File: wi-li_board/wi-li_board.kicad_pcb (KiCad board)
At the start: 2 copper layers, 20.8 x 79.6 mm, 30 parts, among them J1 Barrel_Jack_MountingPin, J2 2059-302/998-403, J3 2059-302/998-403, J4 2059-302/998-403, Q1 Q_NMOS_DGS, Q2 Q_NMOS_DGS, Q3 Q_NMOS_DGS, U1 AP1509, U2 ESP-12E

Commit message: fix issues from first rev
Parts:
- added R10: 330, Resistor_SMD:R_0805_2012Metric_Pad1.20x1.40mm_HandSolder, F.Cu at (149.8, 105.5)
- added R11: 10k, Resistor_SMD:R_0805_2012Metric_Pad1.20x1.40mm_HandSolder, F.Cu at (145.8, 105.5)
- added R9: 10k, Resistor_SMD:R_0805_2012Metric_Pad1.20x1.40mm_HandSolder, F.Cu at (145.8, 97.6)
- L1: footprint Inductor_SMD:L_Vishay_IFSC-1515AH_4x4x1.8mm -> RLC:L_Vishay_IFSC-1515AH_HandSolder
- R1: value 10k -> 330
- R3, R7: value 330 -> 10k
- moved F2 39.5 mm to (150.5, 122.8), turned to 180 degrees
- moved C1 32.3 mm to (138.5, 112.4)
- moved C2 32.3 mm to (140.6, 112.4)
- moved C3 32.3 mm to (145.6, 118.2)
- moved C4 32.3 mm to (145.6, 120.4)
- moved U1 32.3 mm to (144.4, 112.4)
- moved L1 32.1 mm to (139.3, 118.7)
- moved R8 30.7 mm to (148.0, 79.7), turned to 90 degrees
- moved F1 27.8 mm to (135.6, 117.2), turned to -90 degrees
- moved R7 27.7 mm to (145.8, 79.7), turned to 90 degrees
- moved R6 23.7 mm to (150.2, 79.7), turned to 90 degrees
- moved D1 22.2 mm to (135.6, 111.8), turned to 90 degrees
- moved R3 16.0 mm to (141.4, 79.7), turned to 90 degrees
- moved R1 15.1 mm to (149.8, 89.5)
- moved J1 12.6 mm to (143.9, 128.4), turned to 0 degrees
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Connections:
- C1 pad 2: Net-(C1-Pad2) -> Net-(D1-Pad1)
- C2 pad 1: Net-(C1-Pad2) -> Net-(D1-Pad1)
- F1 pad 1: Net-(C1-Pad2) -> Net-(D1-Pad1)
- Q1 pad 1: Net-(F3-Pad1) -> Net-(Q1-Pad1)
- Q1 pad 2: Net-(Q1-Pad2) -> GND
- Q1 pad 3: GND -> Net-(F3-Pad1)
- Q2 pad 1: Net-(F4-Pad1) -> Net-(Q2-Pad1)
- Q2 pad 2: Net-(Q2-Pad2) -> GND
- Q2 pad 3: GND -> Net-(F4-Pad1)
- Q3 pad 1: Net-(F5-Pad1) -> Net-(Q3-Pad1)
- Q3 pad 2: Net-(Q3-Pad2) -> GND
- Q3 pad 3: GND -> Net-(F5-Pad1)
- R1 pad 1: VDD -> Net-(Q1-Pad1)
- R1 pad 2: Net-(R1-Pad2) -> GPIO_4
- R3 pad 1: Net-(Q1-Pad2) -> VDD
- R3 pad 2: GPIO_4 -> Net-(R3-Pad2)
- R4 pad 2: Net-(Q1-Pad2) -> Net-(Q1-Pad1)
- R5 pad 1: Net-(Q2-Pad2) -> Net-(Q2-Pad1)
- R6 pad 2: Net-(Q2-Pad2) -> Net-(R6-Pad2)
- R7 pad 1: Net-(Q3-Pad2) -> VDD
- R7 pad 2: GPIO_14 -> Net-(R7-Pad2)
- R8 pad 1: GND -> VDD
- R8 pad 2: Net-(Q3-Pad2) -> Net-(R8-Pad2)
- U1 pad 1: Net-(C1-Pad2) -> Net-(D1-Pad1)
- U2 pad 1: Net-(R1-Pad2) -> Net-(R2-Pad2)
- U2 pad 13: GPIO_4 -> unconnected-(U2-Pad13)
- U2 pad 14: GPIO_5 -> unconnected-(U2-Pad14)
- U2 pad 15: GPIO_3 -> GND
- U2 pad 16: unconnected-(U2-Pad16) -> Net-(R6-Pad2)
- U2 pad 17: unconnected-(U2-Pad17) -> Net-(R8-Pad2)
- U2 pad 18: unconnected-(U2-Pad18) -> Net-(R7-Pad2)
- U2 pad 19: GPIO9 -> GPIO_4
- U2 pad 20: GPIO10 -> unconnected-(U2-Pad20)
- U2 pad 3: Net-(R2-Pad2) -> Net-(R3-Pad2)
- U2 pad 4: GPIO_16 -> unconnected-(U2-Pad4)
- U2 pad 7: GPIO_13 -> unconnected-(U2-Pad7)
- U2 pad 9: GND -> unconnected-(U2-Pad9)
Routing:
- net VDD: track 13.0 -> 64.7 mm
- net Net-(R1-Pad2): track 28.5 -> 0.00 mm
- net Net-(C1-Pad2): track 20.1 -> 0.00 mm, vias 6 -> 0
- net Net-(R3-Pad2): track 0.00 -> 19.9 mm, vias 0 -> 2
- net Net-(R7-Pad2): track 0.00 -> 14.7 mm, vias 0 -> 2
- net GPIO_4: track 21.7 -> 34.7 mm
- net Net-(R8-Pad2): track 0.00 -> 12.9 mm, vias 0 -> 2
- net Net-(R6-Pad2): track 0.00 -> 11.2 mm, vias 0 -> 2
- net VCC: track 65.7 -> 76.5 mm
- net GND: track 21.1 -> 13.8 mm, vias 24 -> 33
- net GPIO_14: track 50.6 -> 57.8 mm
- net Net-(Q3-Pad2): track 6.06 -> 0.00 mm
- net Net-(Q1-Pad2): track 6.04 -> 0.00 mm
- net Net-(Q2-Pad2): track 5.95 -> 0.00 mm
- net Net-(D1-Pad1): track 12.9 -> 18.0 mm, vias 2 -> 0
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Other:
- board size 20.8 x 79.6 mm -> 25 x 88 mm

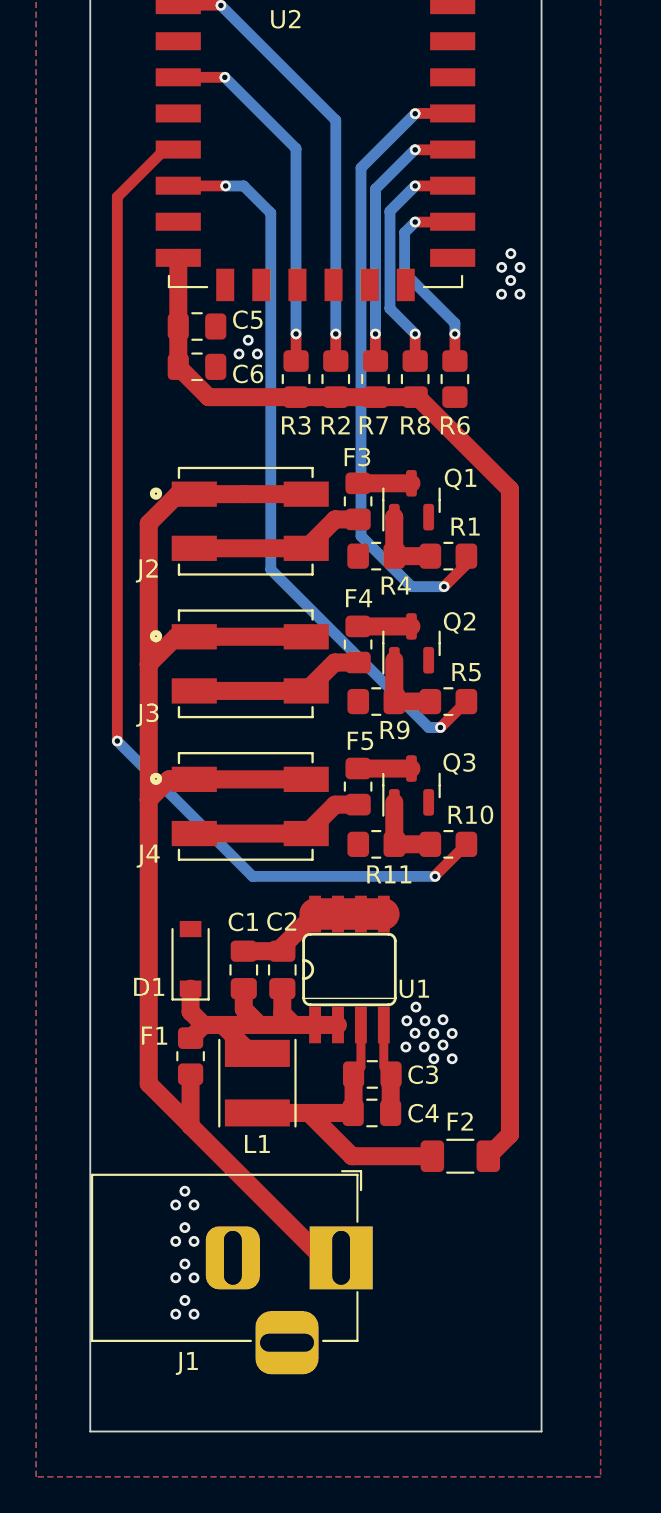
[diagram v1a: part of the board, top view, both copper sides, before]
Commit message: add current measurement and do most of the layout, plus fix voltage regulator mistake
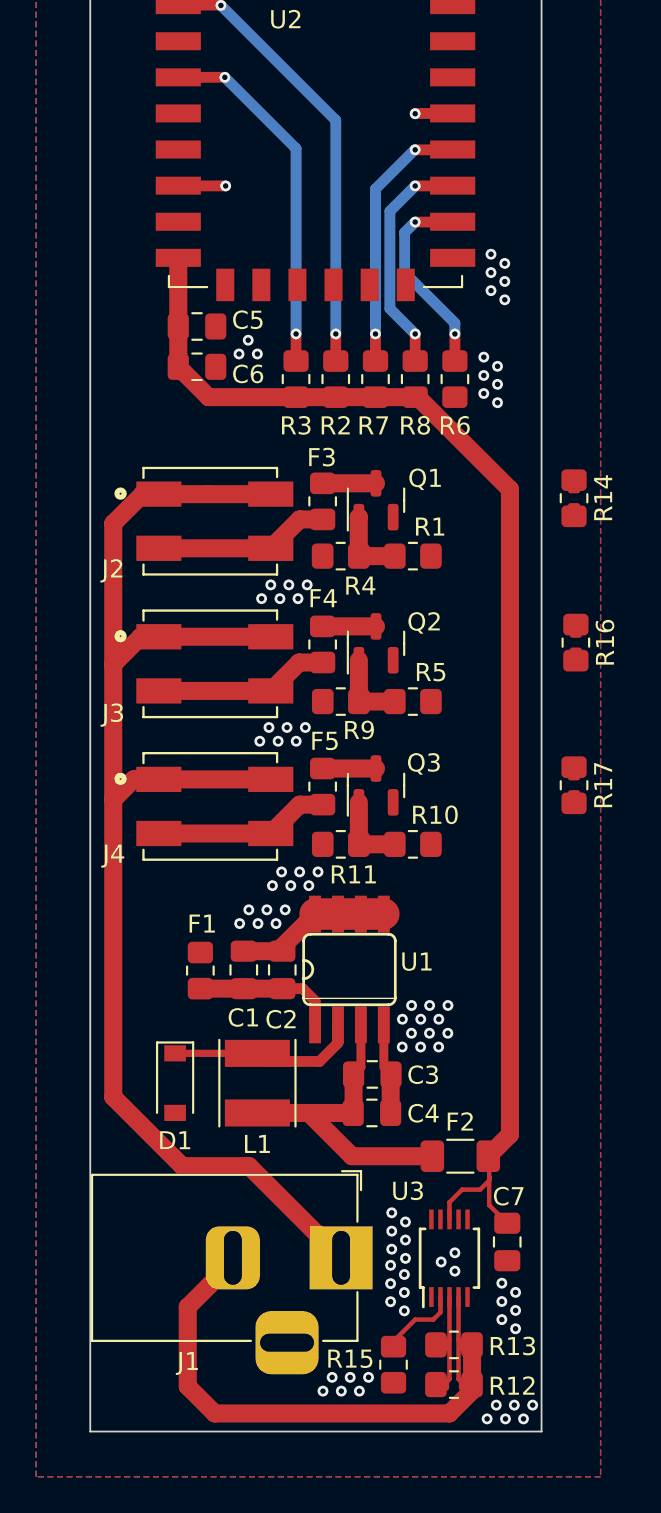
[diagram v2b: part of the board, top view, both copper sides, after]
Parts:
- added C7: 100n, Capacitor_SMD:C_0805_2012Metric_Pad1.18x1.45mm_HandSolder, F.Cu at (153.1, 127.5)
- added R12: 50m, RLC:R_shunt_0805_2012Metric_Pad1.20x1.40mm_HandSolder, F.Cu at (150.2, 135.4)
- added R13: 50m, RLC:R_shunt_0805_2012Metric_Pad1.20x1.40mm_HandSolder, F.Cu at (150.2, 133.2)
- added R14: 50m, RLC:R_shunt_0805_2012Metric_Pad1.20x1.40mm_HandSolder, F.Cu at (156.8, 86.3)
- added R15: 10k, Resistor_SMD:R_0805_2012Metric_Pad1.20x1.40mm_HandSolder, F.Cu at (146.8, 134.3)
- added R16: 50m, RLC:R_shunt_0805_2012Metric_Pad1.20x1.40mm_HandSolder, F.Cu at (156.9, 94.3)
- added R17: 50m, RLC:R_shunt_0805_2012Metric_Pad1.20x1.40mm_HandSolder, F.Cu at (156.8, 102.2)
- added U3: ADS1115IDGS, Package_SO:TSSOP-10_3x3mm_P0.5mm, F.Cu at (149.9, 128.4)
- moved D1 6.94 mm to (134.7, 118.7), turned to -90 degrees
- moved F1 4.77 mm to (136.1, 112.5), turned to 90 degrees
- moved F3 1.96 mm to (142.9, 86.5)
- moved F4 1.96 mm to (142.9, 94.4)
- moved F5 1.96 mm to (142.9, 102.3)
- moved J2 1.96 mm to (136.9, 87.6)
- moved J3 1.96 mm to (136.9, 95.5)
- moved J4 1.96 mm to (136.9, 103.4)
- moved R1 1.96 mm to (147.9, 89.5)
- moved R10 1.96 mm to (147.9, 105.5)
- moved R11 1.96 mm to (143.9, 105.5)
- moved R4 1.96 mm to (143.9, 89.5)
- moved R5 1.96 mm to (147.9, 97.6)
- moved R9 1.96 mm to (143.9, 97.6)
- moved Q1 1.96 mm to (145.8, 86.4)
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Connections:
- net GPIO_12 renamed OUT_CTRL_2
- net GPIO_14 renamed OUT_CTRL_3
- net GPIO_4 renamed OUT_CTRL_1
- C1 pad 2: Net-(D1-Pad1) -> Net-(C1-Pad2)
- C2 pad 1: Net-(D1-Pad1) -> Net-(C1-Pad2)
- F1 pad 1: Net-(D1-Pad1) -> Net-(C1-Pad2)
- J1 pad 2: GND -> Net-(J1-Pad2)
- Q1 pad 2: GND -> Net-(Q1-Pad2)
- Q2 pad 2: GND -> Net-(Q2-Pad2)
- Q3 pad 2: GND -> Net-(Q3-Pad2)
- U1 pad 1: Net-(D1-Pad1) -> Net-(C1-Pad2)
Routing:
- net OUT_CTRL_3: track 57.8 -> 0.00 mm, vias 2 -> 0
- net OUT_CTRL_2: track 40.6 -> 2.63 mm, vias 2 -> 1
- net OUT_CTRL_1: track 34.7 -> 2.08 mm, vias 2 -> 1
- net Net-(J1-Pad2): track 0.00 -> 27.6 mm
- net VDD: track 64.7 -> 72.7 mm
- net Net-(C1-Pad2): track 0.00 -> 7.96 mm
- net Net-(D1-Pad1): track 18.0 -> 10.6 mm
- net I_SENSE_VCC_NEG: track 0.00 -> 5.45 mm, vias 0 -> 6
- net I_SENSE_VCC_POS: track 0.00 -> 5.40 mm
- net Net-(R15-Pad2): track 0.00 -> 4.41 mm
- net VCC: track 76.5 -> 77.1 mm
- net GND: vias 33 -> 78
- added copper zone on B.Cu, net I_SENSE_VCC_NEG
- added copper zone on F.Cu, net I_SENSE_VCC_NEG
- removed copper zone on B.Cu, net GND
- removed copper zone on F.Cu, net GND

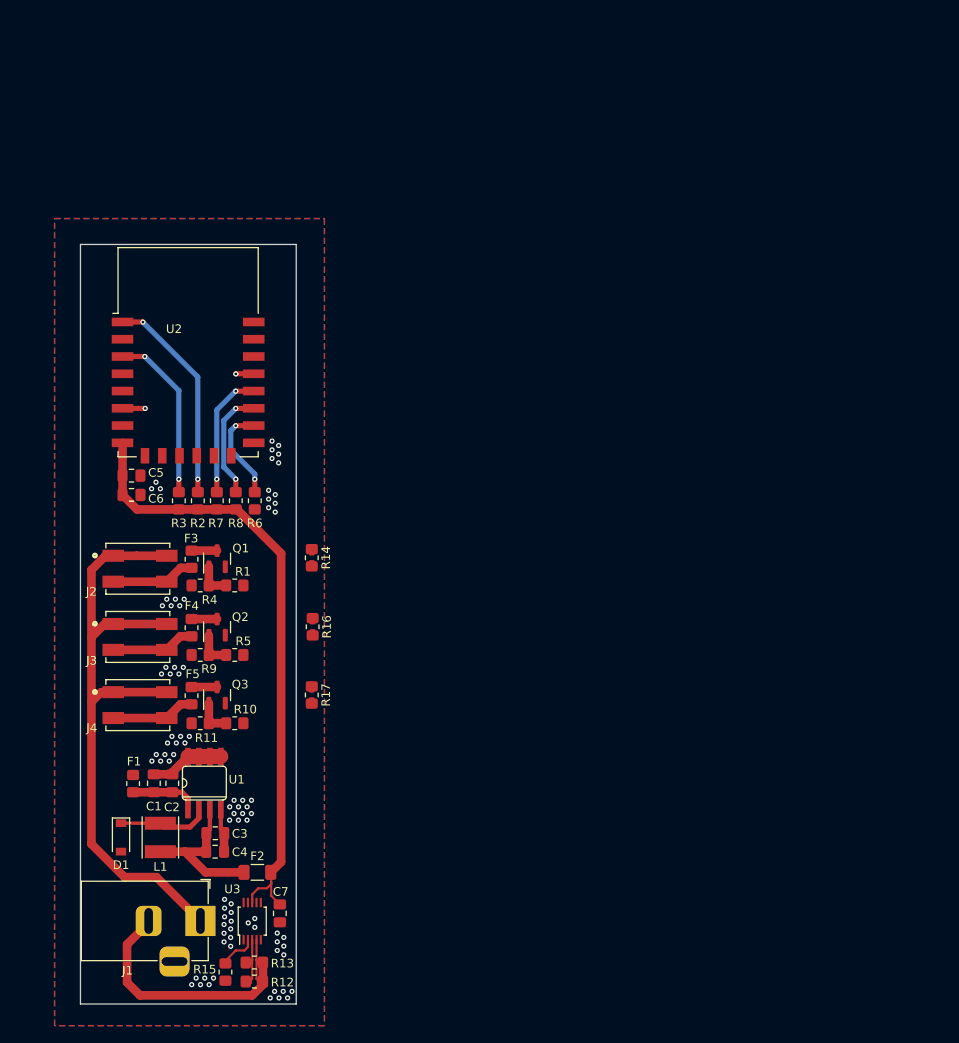
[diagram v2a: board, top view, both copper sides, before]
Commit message: Circular Board   - Fix mistake on voltage regulator from previous version   - Add ADC IC   - Add current measurement to all three channels and input using ADC IC   - Add programming header   - Switch to XT-30 connectors instead of Wago   - Panelize
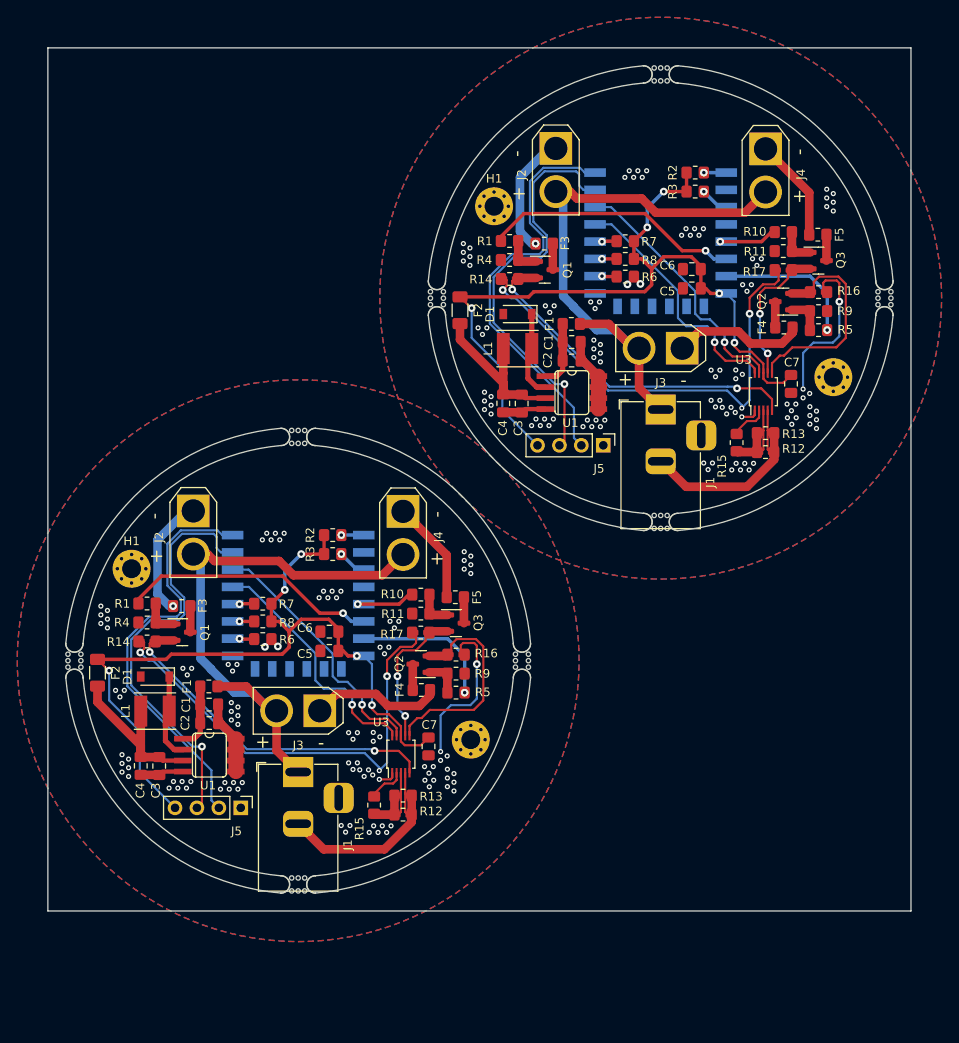
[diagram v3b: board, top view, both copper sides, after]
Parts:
- removed the C1 at (138.5, 112.4)
- removed the C2 at (140.6, 112.4)
- removed the C3 at (145.6, 118.2)
- removed the C4 at (145.6, 120.4)
- removed the C5 at (135.9, 76.8)
- removed the C6 at (135.9, 79.0)
- removed the C7 at (153.1, 127.5)
- removed the D1 at (134.7, 118.7)
- removed the F1 at (136.1, 112.5)
- removed the F2 at (150.5, 122.8)
- removed the L1 at (139.3, 118.7)
- removed the R12 at (150.2, 135.4)
- removed the R13 at (150.2, 133.2)
- removed the R15 at (146.8, 134.3)
- removed the R2 at (143.6, 79.7)
- removed the R3 at (141.4, 79.7)
- removed the R6 at (150.2, 79.7)
- removed the R7 at (145.8, 79.7)
- removed the R8 at (148.0, 79.7)
- removed the U1 at (144.4, 112.4)
- removed the U3 at (149.9, 128.4)
- added C1: 10n, Capacitor_SMD:C_0805_2012Metric_Pad1.18x1.45mm_HandSolder, F.Cu at (186.9, 61.3)
- added C1: 10n, Capacitor_SMD:C_0805_2012Metric_Pad1.18x1.45mm_HandSolder, F.Cu at (144.9, 103.3)
- added C2: 100n, Capacitor_SMD:C_0805_2012Metric_Pad1.18x1.45mm_HandSolder, F.Cu at (144.9, 105.4)
- added C2: 100n, Capacitor_SMD:C_0805_2012Metric_Pad1.18x1.45mm_HandSolder, F.Cu at (186.9, 63.4)
- added C3: 10n, Capacitor_SMD:C_0805_2012Metric_Pad1.18x1.45mm_HandSolder, F.Cu at (139.1, 110.4)
- added C3: 10n, Capacitor_SMD:C_0805_2012Metric_Pad1.18x1.45mm_HandSolder, F.Cu at (181.1, 68.4)
- added C4: 100n, Capacitor_SMD:C_0805_2012Metric_Pad1.18x1.45mm_HandSolder, F.Cu at (137.0, 110.4)
- added C4: 100n, Capacitor_SMD:C_0805_2012Metric_Pad1.18x1.45mm_HandSolder, F.Cu at (179.0, 68.4)
- added C5: 10n, Capacitor_SMD:C_0805_2012Metric_Pad1.18x1.45mm_HandSolder, F.Cu at (200.8, 55.1)
- added C5: 10n, Capacitor_SMD:C_0805_2012Metric_Pad1.18x1.45mm_HandSolder, F.Cu at (158.8, 97.1)
- added C6: 100n, Capacitor_SMD:C_0805_2012Metric_Pad1.18x1.45mm_HandSolder, F.Cu at (200.8, 52.9)
- added C6: 100n, Capacitor_SMD:C_0805_2012Metric_Pad1.18x1.45mm_HandSolder, F.Cu at (158.8, 94.9)
- added C7: 100n, Capacitor_SMD:C_0805_2012Metric_Pad1.18x1.45mm_HandSolder, F.Cu at (212.3, 66.2)
- added C7: 100n, Capacitor_SMD:C_0805_2012Metric_Pad1.18x1.45mm_HandSolder, F.Cu at (170.3, 108.2)
- added D1: MBRX120LF-TP, Diode_SMD:D_SOD-123, F.Cu at (138.6, 100.1)
- added D1: MBRX120LF-TP, Diode_SMD:D_SOD-123, F.Cu at (180.6, 58.1)
- added F1: 375m, Resistor_SMD:R_0805_2012Metric_Pad1.20x1.40mm_HandSolder, F.Cu at (186.9, 59.2)
- added F1: 375m, Resistor_SMD:R_0805_2012Metric_Pad1.20x1.40mm_HandSolder, F.Cu at (144.9, 101.2)
- added F2: 160m, Resistor_SMD:R_1206_3216Metric_Pad1.30x1.75mm_HandSolder, F.Cu at (174.0, 57.6)
- added F2: 160m, Resistor_SMD:R_1206_3216Metric_Pad1.30x1.75mm_HandSolder, F.Cu at (132.0, 99.6)
- added F3: 375m, Resistor_SMD:R_0805_2012Metric_Pad1.20x1.40mm_HandSolder, F.Cu at (183.7, 49.9)
- added F4: 375m, Resistor_SMD:R_0805_2012Metric_Pad1.20x1.40mm_HandSolder, F.Cu at (211.5, 59.6)
- added F5: 375m, Resistor_SMD:R_0805_2012Metric_Pad1.20x1.40mm_HandSolder, F.Cu at (215.4, 48.9)
- added H1: MountingHole_Pad, MountingHole:MountingHole_2.2mm_M2_Pad_Via, F.Cu at (135.9, 87.6)
- added H1: MountingHole_Pad, MountingHole:MountingHole_2.2mm_M2_Pad_Via, F.Cu at (177.9, 45.6)
- added H2: MountingHole_Pad, MountingHole:MountingHole_2.2mm_M2_Pad_Via, F.Cu at (217.2, 65.4)
- added H2: MountingHole_Pad, MountingHole:MountingHole_2.2mm_M2_Pad_Via, F.Cu at (175.2, 107.4)
- added J1: Barrel_Jack_MountingPin, Connector_BarrelJack:BarrelJack_Horizontal, F.Cu at (197.2, 69.1)
- added J2: XT30, Connector_AMASS:AMASS_XT30U-M_1x02_P5.0mm_Vertical, F.Cu at (185.1, 38.9)
- added J3: XT30, Connector_AMASS:AMASS_XT30U-M_1x02_P5.0mm_Vertical, F.Cu at (199.7, 62.0)
- added J4: XT30, Connector_AMASS:AMASS_XT30U-M_1x02_P5.0mm_Vertical, F.Cu at (209.4, 38.9)
- added J5: DBG, Connector_PinHeader_2.54mm:PinHeader_1x04_P2.54mm_Vertical, F.Cu at (190.6, 73.3)
- added J5: DBG, Connector_PinHeader_2.54mm:PinHeader_1x04_P2.54mm_Vertical, F.Cu at (148.6, 115.3)
- added L1: 47u, RLC:L_Vishay_IFSC-1515AH_HandSolder, F.Cu at (180.6, 62.1)
- added L1: 47u, RLC:L_Vishay_IFSC-1515AH_HandSolder, F.Cu at (138.6, 104.1)
- added Q1: Q_NMOS_DGS, Package_TO_SOT_SMD:SOT-23, F.Cu at (183.8, 52.9)
- added Q2: Q_NMOS_DGS, Package_TO_SOT_SMD:SOT-23, F.Cu at (211.4, 56.6)
- added Q3: Q_NMOS_DGS, Package_TO_SOT_SMD:SOT-23, F.Cu at (215.5, 51.9)
- added R1: 330, Resistor_SMD:R_0805_2012Metric_Pad1.20x1.40mm_HandSolder, F.Cu at (179.7, 49.6)
- added R10: 330, Resistor_SMD:R_0805_2012Metric_Pad1.20x1.40mm_HandSolder, F.Cu at (211.4, 48.6)
- added R11: 10k, Resistor_SMD:R_0805_2012Metric_Pad1.20x1.40mm_HandSolder, F.Cu at (211.4, 50.8)
- added R12: 50m, RLC:R_shunt_0805_2012Metric_Pad1.20x1.40mm_HandSolder, F.Cu at (167.4, 116.1)
- added R12: 50m, RLC:R_shunt_0805_2012Metric_Pad1.20x1.40mm_HandSolder, F.Cu at (209.4, 74.1)
- added R13: 50m, RLC:R_shunt_0805_2012Metric_Pad1.20x1.40mm_HandSolder, F.Cu at (167.4, 113.9)
- added R13: 50m, RLC:R_shunt_0805_2012Metric_Pad1.20x1.40mm_HandSolder, F.Cu at (209.4, 71.9)
- added R14: 50m, RLC:R_shunt_0805_2012Metric_Pad1.20x1.40mm_HandSolder, F.Cu at (179.7, 54.0)
- added R15: 10k, Resistor_SMD:R_0805_2012Metric_Pad1.20x1.40mm_HandSolder, F.Cu at (164.0, 115.0)
- added R15: 10k, Resistor_SMD:R_0805_2012Metric_Pad1.20x1.40mm_HandSolder, F.Cu at (206.0, 73.0)
- added R16: 50m, RLC:R_shunt_0805_2012Metric_Pad1.20x1.40mm_HandSolder, F.Cu at (215.5, 55.5)
- added R17: 50m, RLC:R_shunt_0805_2012Metric_Pad1.20x1.40mm_HandSolder, F.Cu at (211.4, 53.0)
- added R2: 10k, Resistor_SMD:R_0805_2012Metric_Pad1.20x1.40mm_HandSolder, F.Cu at (159.2, 83.7)
- added R2: 10k, Resistor_SMD:R_0805_2012Metric_Pad1.20x1.40mm_HandSolder, F.Cu at (201.2, 41.7)
- added R3: 10k, Resistor_SMD:R_0805_2012Metric_Pad1.20x1.40mm_HandSolder, F.Cu at (201.2, 43.9)
- added R3: 10k, Resistor_SMD:R_0805_2012Metric_Pad1.20x1.40mm_HandSolder, F.Cu at (159.2, 85.9)
- added R4: 10k, Resistor_SMD:R_0805_2012Metric_Pad1.20x1.40mm_HandSolder, F.Cu at (179.7, 51.8)
- added R5: 330, Resistor_SMD:R_0805_2012Metric_Pad1.20x1.40mm_HandSolder, F.Cu at (215.5, 59.9)
- added R6: 10k, Resistor_SMD:R_0805_2012Metric_Pad1.20x1.40mm_HandSolder, F.Cu at (151.1, 95.7)
- added R6: 10k, Resistor_SMD:R_0805_2012Metric_Pad1.20x1.40mm_HandSolder, F.Cu at (193.1, 53.7)
- added R7: 10k, Resistor_SMD:R_0805_2012Metric_Pad1.20x1.40mm_HandSolder, F.Cu at (151.1, 91.6)
- added R7: 10k, Resistor_SMD:R_0805_2012Metric_Pad1.20x1.40mm_HandSolder, F.Cu at (193.1, 49.6)
- added R8: 10k, Resistor_SMD:R_0805_2012Metric_Pad1.20x1.40mm_HandSolder, F.Cu at (193.1, 51.7)
- added R8: 10k, Resistor_SMD:R_0805_2012Metric_Pad1.20x1.40mm_HandSolder, F.Cu at (151.1, 93.7)
- added R9: 10k, Resistor_SMD:R_0805_2012Metric_Pad1.20x1.40mm_HandSolder, F.Cu at (215.5, 57.7)
- added U1: AP1509, Diodes_Inc:SO08, F.Cu at (144.9, 109.2)
- added U1: AP1509, Diodes_Inc:SO08, F.Cu at (186.9, 67.2)
- added U2: ESP-12E, RF_Module:ESP-12E, B.Cu at (197.2, 45.2)
- added U3: ADS1115IDGS, Package_SO:TSSOP-10_3x3mm_P0.5mm, F.Cu at (167.1, 109.1)
- added U3: ADS1115IDGS, Package_SO:TSSOP-10_3x3mm_P0.5mm, F.Cu at (209.1, 67.1)
- added mouse-bite-2mm-slot: VAL**, Panelization:mouse-bite-2mm-slot, F.Cu at (197.2, 82.2)
- added mouse-bite-2mm-slot: VAL**, Panelization:mouse-bite-2mm-slot, F.Cu at (171.3, 56.2)
- added mouse-bite-2mm-slot: VAL**, Panelization:mouse-bite-2mm-slot, F.Cu at (155.2, 124.2)
- added mouse-bite-2mm-slot: VAL**, Panelization:mouse-bite-2mm-slot, F.Cu at (181.2, 98.2)
- added mouse-bite-2mm-slot: VAL**, Panelization:mouse-bite-2mm-slot, F.Cu at (223.2, 56.2)
- added mouse-bite-2mm-slot: VAL**, Panelization:mouse-bite-2mm-slot, F.Cu at (197.2, 30.3)
- added mouse-bite-2mm-slot: VAL**, Panelization:mouse-bite-2mm-slot, F.Cu at (155.2, 72.3)
- added mouse-bite-2mm-slot: VAL**, Panelization:mouse-bite-2mm-slot, F.Cu at (129.3, 98.2)
- J2, J3, J4: value 2059-302/998-403 -> XT30; footprint Wago:WAGO_2059-302_998-403 -> Connector_AMASS:AMASS_XT30U-M_1x02_P5.0mm_Vertical
- U2: moved to B.Cu
- moved J4 37.9 mm to (167.4, 80.9), turned to -90 degrees
- moved F5 32.6 mm to (173.4, 90.9), turned to 180 degrees
- moved R9 29.7 mm to (173.5, 99.7), turned to 180 degrees
- moved Q3 28.9 mm to (173.5, 93.9), turned to 0 degrees
- moved R11 28.5 mm to (169.4, 92.8)
- moved U2 27.8 mm to (155.2, 87.2), turned to 180 degrees
- moved F4 27.6 mm to (169.5, 101.6), turned to 0 degrees
- moved R10 26.2 mm to (169.4, 90.6), turned to 180 degrees
- moved R5 26.0 mm to (173.5, 101.9)
- moved Q2 24.0 mm to (169.4, 98.6), turned to 180 degrees
- moved J3 22.5 mm to (157.7, 104.0), turned to 180 degrees
- moved R14 21.4 mm to (137.7, 96.0), turned to 0 degrees
- moved J1 20.6 mm to (155.2, 111.1), turned to 90 degrees
- moved R16 16.9 mm to (173.5, 97.5), turned to 180 degrees
- moved R17 14.6 mm to (169.4, 95.0), turned to 0 degrees
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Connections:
- J2 pad 1: VCC -> Net-(F3-Pad2)
- J2 pad 2: Net-(F3-Pad2) -> VCC
- J3 pad 1: VCC -> Net-(F4-Pad2)
- J3 pad 2: Net-(F4-Pad2) -> VCC
- J4 pad 1: VCC -> Net-(F5-Pad2)
- J4 pad 2: Net-(F5-Pad2) -> VCC
- U2 pad 19: OUT_CTRL_1 -> SCL
- U2 pad 20: unconnected-(U2-Pad20) -> SDA
- U2 pad 21: unconnected-(U2-Pad21) -> RX
- U2 pad 22: unconnected-(U2-Pad22) -> TX
- U2 pad 6: OUT_CTRL_2 -> OUT_CTRL_1
- U2 pad 7: unconnected-(U2-Pad7) -> OUT_CTRL_2
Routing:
- net GND: track 13.8 -> 196.4 mm, vias 78 -> 214
- net VDD: track 72.7 -> 180.2 mm, vias 0 -> 10
- net RX: track 0.00 -> 98.3 mm, vias 0 -> 2
- net TX: track 0.00 -> 97.0 mm
- net Net-(Q1-Pad2): track 0.00 -> 80.5 mm, vias 0 -> 4
- net SDA: track 0.00 -> 60.0 mm, vias 0 -> 2
- net SCL: track 0.00 -> 57.8 mm, vias 0 -> 2
- net OUT_CTRL_1: track 2.08 -> 59.8 mm, vias 1 -> 2
- net VCC: track 77.1 -> 132.5 mm
- net I_SENSE_MOS_2: track 0.00 -> 49.7 mm
- net Net-(Q3-Pad2): track 0.00 -> 33.5 mm, vias 0 -> 4
- net OUT_CTRL_2: track 2.63 -> 33.6 mm, vias 1 -> 2
- net Net-(C3-Pad2): track 18.2 -> 41.2 mm
- net Net-(F4-Pad2): track 9.73 -> 30.6 mm
- net Net-(J1-Pad2): track 27.6 -> 48.3 mm
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- added copper zone on B.Cu, net GND
- added copper zone on F.Cu, net GND
- removed copper zone on B.Cu, net I_SENSE_VCC_NEG
- removed copper zone on F.Cu, net I_SENSE_VCC_NEG
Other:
- board size 25 x 88 mm -> 100 x 100 mm
